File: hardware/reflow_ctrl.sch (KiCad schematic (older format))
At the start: 36 parts, among them IC1 MAX6675, IC2 ATXMEGA128A4U-A, P1 CONN_01X06, P2 CONN_01X02, U1 LT1129CST-3.3, U2 MOC3063, U3 BTA41/600B, X1 USB-Mini-B, X2 Mains, X3 Load

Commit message: Add and assign mains terminal footprint
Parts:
- X2, X3: footprint (none) -> uMIDI:Mains_Solder
- X4: renamed from P2; value CONN_01X02 -> Thermocouple; footprint (none) -> uMIDI:Pinhead1-2
- gave numbers to parts that had none: 1
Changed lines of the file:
@@
 	6300 2450 6500 2450
 $Comp
-L GND #PWR01
+L GND #PWR20
 U 1 1 56A9FAD0
 P 6450 2700
-F 0 "#PWR01" H 6450 2450 50  0001 C CNN
+F 0 "#PWR20" H 6450 2450 50  0001 C CNN
 F 1 "GND" H 6450 2550 50  0000 C CNN
 F 2 "" H 6450 2700 60  0000 C CNN
@@
 $EndComp
 $Comp
-L GND #PWR02
+L GND #PWR22
 U 1 1 56AA0C93
 P 8200 5000
-F 0 "#PWR02" H 8200 4750 50  0001 C CNN
+F 0 "#PWR22" H 8200 4750 50  0001 C CNN
 F 1 "GND" H 8200 4850 50  0000 C CNN
 F 2 "" H 8200 5000 60  0000 C CNN
@@
 	8100 4950 8350 4950
 $Comp
-L +5V #PWR03
+L +5V #PWR21
 U 1 1 56AA1098
 P 8200 4600
-F 0 "#PWR03" H 8200 4450 50  0001 C CNN
+F 0 "#PWR21" H 8200 4450 50  0001 C CNN
 F 1 "+5V" H 8200 4740 50  0000 C CNN
 F 2 "" H 8200 4600 60  0000 C CNN
@@
 U 1 1 56AA462E
 P 8350 4800
-F 0 "C11" H 8250 4700 50  0000 L CNN
-F 1 "100n" H 8100 4900 50  0000 L CNN
+F 0 "C11" H 8350 4900 50  0000 L CNN
+F 1 "100n" H 8350 4700 50  0000 L CNN
 F 2 "Capacitors_SMD:C_0603" H 8388 4650 30  0001 C CNN
 F 3 "" H 8350 4800 60  0001 C CNN
@@
 	2550 2550 2000 2550
 $Comp
-L GND #PWR04
+L GND #PWR5
 U 1 1 56AE5967
 P 2050 3100
-F 0 "#PWR04" H 2050 2850 50  0001 C CNN
+F 0 "#PWR5" H 2050 2850 50  0001 C CNN
 F 1 "GND" H 2050 2950 50  0001 C CNN
 F 2 "" H 2050 3100 60  0000 C CNN
@@
 NoConn ~ 2000 2850
 $Comp
-L GND #PWR05
+L GND #PWR17
 U 1 1 56AE5F8B
 P 3500 5200
-F 0 "#PWR05" H 3500 4950 50  0001 C CNN
+F 0 "#PWR17" H 3500 4950 50  0001 C CNN
 F 1 "GND" H 3500 5050 50  0001 C CNN
 F 2 "" H 3500 5200 60  0000 C CNN
@@
 $EndComp
 $Comp
-L GND #PWR06
+L GND #PWR11
 U 1 1 56AEA13C
 P 2450 2400
-F 0 "#PWR06" H 2450 2150 50  0001 C CNN
+F 0 "#PWR11" H 2450 2150 50  0001 C CNN
 F 1 "GND" H 2450 2250 50  0001 C CNN
 F 2 "" H 2450 2400 60  0000 C CNN
@@
 $EndComp
 $Comp
-L GND #PWR07
+L GND #PWR13
 U 1 1 56AEAD9B
 P 2800 2400
-F 0 "#PWR07" H 2800 2150 50  0001 C CNN
+F 0 "#PWR13" H 2800 2150 50  0001 C CNN
 F 1 "GND" H 2800 2250 50  0001 C CNN
 F 2 "" H 2800 2400 60  0000 C CNN
@@
 $EndComp
 $Comp
-L GND #PWR08
+L GND #PWR15
 U 1 1 56AEADF6
 P 3050 2400
-F 0 "#PWR08" H 3050 2150 50  0001 C CNN
+F 0 "#PWR15" H 3050 2150 50  0001 C CNN
 F 1 "GND" H 3050 2250 50  0001 C CNN
 F 2 "" H 3050 2400 60  0000 C CNN
@@
 $EndComp
 $Comp
-L GND #PWR09
+L GND #PWR16
 U 1 1 56AEAE51
 P 3300 2400
-F 0 "#PWR09" H 3300 2150 50  0001 C CNN
+F 0 "#PWR16" H 3300 2150 50  0001 C CNN
 F 1 "GND" H 3300 2250 50  0001 C CNN
 F 2 "" H 3300 2400 60  0000 C CNN
@@
 	3700 1950 3800 1950
 $Comp
-L GND #PWR010
+L GND #PWR18
 U 1 1 56AEE788
 P 3950 2400
-F 0 "#PWR010" H 3950 2150 50  0001 C CNN
+F 0 "#PWR18" H 3950 2150 50  0001 C CNN
 F 1 "GND" H 3950 2250 50  0001 C CNN
 F 2 "" H 3950 2400 60  0000 C CNN
@@
 $EndComp
 $Comp
-L GND #PWR011
+L GND #PWR19
 U 1 1 56AEE817
 P 4200 2400
-F 0 "#PWR011" H 4200 2150 50  0001 C CNN
+F 0 "#PWR19" H 4200 2150 50  0001 C CNN
 F 1 "GND" H 4200 2250 50  0001 C CNN
 F 2 "" H 4200 2400 60  0000 C CNN
@@
 $EndComp
 $Comp
-L +3.3V #PWR012
+L +3.3V #PWR7
 U 1 1 56AEE96E
 P 2150 1250
-F 0 "#PWR012" H 2150 1100 50  0001 C CNN
+F 0 "#PWR7" H 2150 1100 50  0001 C CNN
 F 1 "+3.3V" H 2150 1390 50  0000 C CNN
 F 2 "" H 2150 1250 60  0000 C CNN
@@
 $EndComp
 $Comp
-L GND #PWR013
+L GND #PWR4
 U 1 1 56AF308D
 P 1800 5700
-F 0 "#PWR013" H 1800 5450 50  0001 C CNN
+F 0 "#PWR4" H 1800 5450 50  0001 C CNN
 F 1 "GND" H 1800 5550 50  0001 C CNN
 F 2 "" H 1800 5700 60  0000 C CNN
@@
 $EndComp
 $Comp
-L GND #PWR014
+L GND #PWR6
 U 1 1 56AF30DC
 P 2100 5700
-F 0 "#PWR014" H 2100 5450 50  0001 C CNN
+F 0 "#PWR6" H 2100 5450 50  0001 C CNN
 F 1 "GND" H 2100 5550 50  0001 C CNN
 F 2 "" H 2100 5700 60  0000 C CNN
@@
 $EndComp
 $Comp
-L GND #PWR015
+L GND #PWR10
 U 1 1 56AF3117
 P 2400 5700
-F 0 "#PWR015" H 2400 5450 50  0001 C CNN
+F 0 "#PWR10" H 2400 5450 50  0001 C CNN
 F 1 "GND" H 2400 5550 50  0001 C CNN
 F 2 "" H 2400 5700 60  0000 C CNN
@@
 	1750 4600 1750 4550
 $Comp
-L GND #PWR016
+L GND #PWR2
 U 1 1 56AF578E
 P 1700 5000
-F 0 "#PWR016" H 1700 4750 50  0001 C CNN
+F 0 "#PWR2" H 1700 4750 50  0001 C CNN
 F 1 "GND" H 1700 4850 50  0001 C CNN
 F 2 "" H 1700 5000 60  0000 C CNN
@@
 	1200 5650 1200 5600
 $Comp
-L GND #PWR017
+L GND #PWR1
 U 1 1 56AF75D9
 P 1300 5700
-F 0 "#PWR017" H 1300 5450 50  0001 C CNN
+F 0 "#PWR1" H 1300 5450 50  0001 C CNN
 F 1 "GND" H 1300 5550 50  0001 C CNN
 F 2 "" H 1300 5700 60  0000 C CNN
@@
 Connection ~ 1800 4600
 $Comp
-L GND #PWR018
+L GND #PWR9
 U 1 1 56AF8D20
 P 2250 4600
-F 0 "#PWR018" H 2250 4350 50  0001 C CNN
+F 0 "#PWR9" H 2250 4350 50  0001 C CNN
 F 1 "GND" H 2250 4450 50  0001 C CNN
 F 2 "" H 2250 4600 60  0000 C CNN
@@
 $EndComp
 $Comp
-L GND #PWR019
+L GND #PWR8
 U 1 1 56AFB955
 P 2200 7500
-F 0 "#PWR019" H 2200 7250 50  0001 C CNN
+F 0 "#PWR8" H 2200 7250 50  0001 C CNN
 F 1 "GND" H 2200 7350 50  0001 C CNN
 F 2 "" H 2200 7500 60  0000 C CNN
@@
 	2200 7500 2200 7450
 $Comp
-L GND #PWR020
+L GND #PWR3
 U 1 1 56AFBD16
 P 1700 7500
-F 0 "#PWR020" H 1700 7250 50  0001 C CNN
+F 0 "#PWR3" H 1700 7250 50  0001 C CNN
 F 1 "GND" H 1700 7350 50  0001 C CNN
 F 2 "" H 1700 7500 60  0000 C CNN
@@
 $EndComp
 $Comp
-L GND #PWR021
+L GND #PWR12
 U 1 1 56AFBD84
 P 2700 7500
-F 0 "#PWR021" H 2700 7250 50  0001 C CNN
+F 0 "#PWR12" H 2700 7250 50  0001 C CNN
 F 1 "GND" H 2700 7350 50  0001 C CNN
 F 2 "" H 2700 7500 60  0000 C CNN
@@
 Connection ~ 2700 7100
 $Comp
-L +3.3V #PWR022
+L +3.3V #PWR14
 U 1 1 56AFC77E
 P 2850 7100
-F 0 "#PWR022" H 2850 6950 50  0001 C CNN
+F 0 "#PWR14" H 2850 6950 50  0001 C CNN
 F 1 "+3.3V" H 2850 7240 50  0000 C CNN
 F 2 "" H 2850 7100 60  0000 C CNN
@@
 $EndComp
 $Comp
-L PWR_FLAG #FLG023
+L PWR_FLAG #FLG1
 U 1 1 56AFC903
 P 1600 7050
-F 0 "#FLG023" H 1600 7145 50  0001 C CNN
+F 0 "#FLG1" H 1600 7145 50  0001 C CNN
 F 1 "PWR_FLAG" H 1600 7230 50  0000 C CNN
 F 2 "" H 1600 7050 60  0000 C CNN
@@
 $EndComp
 $Comp
-L PWR_FLAG #FLG024
+L PWR_FLAG #FLG2
 U 1 1 56AFCDDC
 P 2800 7050
-F 0 "#FLG024" H 2800 7145 50  0001 C CNN
+F 0 "#FLG2" H 2800 7145 50  0001 C CNN
 F 1 "PWR_FLAG" H 2800 7230 50  0000 C CNN
 F 2 "" H 2800 7050 60  0000 C CNN
@@
 F 0 "X2" H 10200 2200 50  0000 C CNN
 F 1 "Mains" V 10300 2000 50  0000 C CNN
-F 2 "" H 10200 2000 60  0000 C CNN
+F 2 "uMIDI:Mains_Solder" H 10200 2000 60  0001 C CNN
 F 3 "" H 10200 2000 60  0000 C CNN
 	1    10200 2000
@@
 F 0 "X3" H 10200 3500 50  0000 C CNN
 F 1 "Load" V 10300 3300 50  0000 C CNN
-F 2 "" H 10200 3300 60  0000 C CNN
+F 2 "uMIDI:Mains_Solder" H 10200 3300 60  0001 C CNN
 F 3 "" H 10200 3300 60  0000 C CNN
 	1    10200 3300
@@
 	9500 3400 10000 3400
 $Comp
-L CONN_01X02 P2
+L CONN_01X02 X4
 U 1 1 56B0080E
 P 9300 4800
-F 0 "P2" H 9300 4950 50  0000 C CNN
-F 1 "CONN_01X02" V 9400 4800 50  0000 C CNN
-F 2 "" H 9300 4800 60  0000 C CNN
+F 0 "X4" H 9300 4950 50  0000 C CNN
+F 1 "Thermocouple" V 9400 4800 50  0000 C CNN
+F 2 "uMIDI:Pinhead1-2" H 9300 4800 60  0001 C CNN
 F 3 "" H 9300 4800 60  0000 C CNN
 	1    9300 4800
@@
 PWR
 $Comp
-L R R?
+L R R7
 U 1 1 56AE5095
 P 8750 2950
-F 0 "R?" V 8830 2950 50  0000 C CNN
+F 0 "R7" V 8830 2950 50  0000 C CNN
 F 1 "47" V 8750 2950 50  0000 C CNN
 F 2 "Resistors_SMD:R_1206" V 8680 2950 30  0001 C CNN

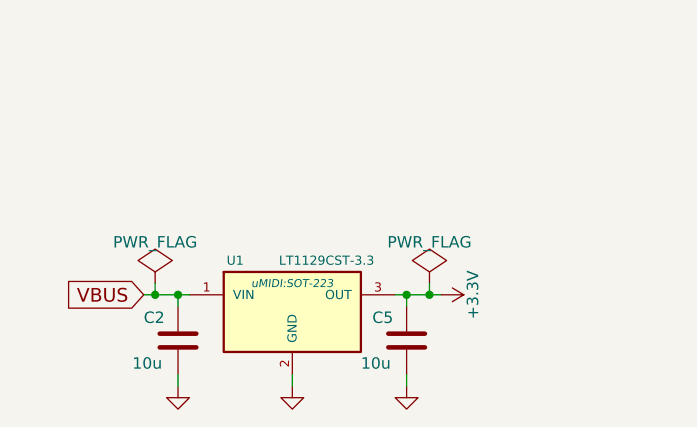
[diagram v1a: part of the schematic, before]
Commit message: Add supplier links and optotriac footprint
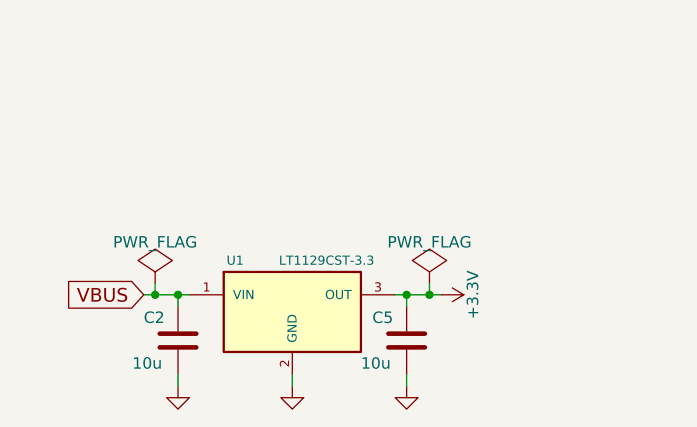
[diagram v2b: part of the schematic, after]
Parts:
- U1: Manufacturer (none) -> Linear Technology; Manufacturer Part Number (none) -> LT1129CST-3.3#PBF; Supplier (none) -> Digikey; Supplier Link (none) -> https://www.digikey.de/product-detail/de/LT1129CST-3.3%23PB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; Supplier Part Number (none) -> LT1129CST-3.3#PBF-ND
- U2: footprint (none) -> uMIDI:MOC3063_SMT; Manufacturer (none) -> Fairchild Semiconductor; Manufacturer Part Number (none) -> MOC3063SR2VM; Supplier (none) -> Digikey; Supplier Link (none) -> http://www.digikey.de/product-detail/de/MOC3063SR2VM/MOC306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; Supplier Part Number (none) -> MOC3063SR2VMCT-ND
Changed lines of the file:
@@
 F 0 "U2" H 6600 2750 50  0000 L CNN
 F 1 "MOC3063" H 6600 2350 50  0000 L CNN
-F 2 "" H 6800 2550 50  0000 L CIN
-F 3 "" H 6775 2550 50  0000 L CNN
+F 2 "uMIDI:MOC3063_SMT" H 6800 2550 50  0001 L CIN
+F 3 "https://www.fairchildsemi.com/datasheets/MO/MOC3061M.pdf" H 6775 2550 50  0001 L CNN
+F 4 "MOC3063SR2VM" H 6600 2750 50  0001 L CNN "Manufacturer Part Number"
+F 5 "MOC3063SR2VMCT-ND" H 6600 2750 50  0001 L CNN "Supplier Part Number"
+F 6 "Fairchild Semiconductor" H 6600 2750 50  0001 L CNN "Manufacturer"
+F 7 "Digikey" H 6600 2750 50  0001 L CNN "Supplier"
+F 8 "http://www.digikey.de/product-detail/de/MOC3063SR2VM/MOC3063SR2VMCT-ND/2094175" H 6600 2750 50  0001 L CNN "Supplier Link"
 	1    6800 2550
 	1    0    0    -1
@@
 F 0 "U1" H 1950 7350 40  0000 C CNN
 F 1 "LT1129CST-3.3" H 2350 7350 40  0000 C CNN
-F 2 "uMIDI:SOT-223" H 2200 7250 35  0000 C CIN
-F 3 "" H 2200 7150 60  0000 C CNN
+F 2 "uMIDI:SOT-223" H 2200 7250 35  0001 C CIN
+F 3 "http://cds.linear.com/docs/en/datasheet/112935ff.pdf" H 2200 7150 60  0001 C CNN
+F 4 "https://www.digikey.de/product-detail/de/LT1129CST-3.3%23PBF/LT1129CST-3.3%23PBF-ND/889181" H 1950 7350 40  0001 C CNN "Supplier Link"
+F 5 "Linear Technology" H 1950 7350 40  0001 C CNN "Manufacturer"
+F 6 "Digikey" H 1950 7350 40  0001 C CNN "Supplier"
+F 7 "LT1129CST-3.3#PBF-ND" H 1950 7350 40  0001 C CNN "Supplier Part Number"
+F 8 "LT1129CST-3.3#PBF" H 1950 7350 40  0001 C CNN "Manufacturer Part Number"
 	1    2200 7150
 	1    0    0    -1

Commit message: Sanetize output circuit; Add varistor
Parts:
- removed L3: 1.5m, symbol INDUCTOR_SMALL
- removed R7: 47, Resistors_SMD:R_1206, symbol R
- added VR1: 430V, Varistors:RV_Disc_D21.5_W5.1_P10, symbol VR
- F1: value F_Small -> Insert 12A slow; footprint (none) -> Fuse_Holders_and_Fuses:Fuseholder5x20_horiz_open_universal_Type-III; Manufacturer (none) -> Schurter Inc.; Manufacturer Part Number (none) -> 0031.8231; Rated Current (none) -> 10A; Supplier (none) -> Digikey; Supplier Link (none) -> http://www.digikey.de/product-detail/de/0031.8231/486-1261-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; Supplier Part Number (none) -> 486-1261-ND
- R4, R5: footprint (none) -> Resistors_SMD:R_1206
- R6: value 47 -> 39
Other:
- moved on the sheet: C12, F1, R6, X2, X3

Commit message: Add fuse holder footprint
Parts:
- F1: footprint Fuse_Holders_and_Fuses:Fuseholder5x20_horiz_open_universal_Type-III -> uMIDI:Fuseholder_Schurter_20x5
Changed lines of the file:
@@
 F 0 "F1" H 9610 1960 50  0000 L CNN
 F 1 "Insert 12A slow" H 9350 1800 50  0000 L CNN
-F 2 "Fuse_Holders_and_Fuses:Fuseholder5x20_horiz_open_universal_Type-III" H 9650 1900 60  0001 C CNN
+F 2 "uMIDI:Fuseholder_Schurter_20x5" H 9650 1900 60  0001 C CNN
 F 3 "http://www.schurterinc.com/var/schurter/storage/ilcatalogue/files/document/datasheet/en/pdf/typ_OGD.pdf" H 9650 1900 60  0001 C CNN
 F 4 "Schurter Inc." H 9610 1960 50  0001 L CNN "Manufacturer"

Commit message: Assign all footprints
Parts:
- C1, L1, L2: footprint (none) -> Capacitors_SMD:C_0603
- IC1: footprint (none) -> Housings_SOIC:SOIC-8_3.9x4.9mm_Pitch1.27mm
- P1: value CONN_01X06 -> PDI; footprint (none) -> Pin_Headers:Pin_Header_Straight_2x03
- R1, R2: footprint (none) -> Resistors_SMD:R_0603
- R3: value TBD -> 390; footprint (none) -> Resistors_SMD:R_0603
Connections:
- wire segments 89 -> 90
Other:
- note added: "Nominal trigger current: 5mA (60mA max)"
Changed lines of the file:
@@
 P 6150 2450
 F 0 "R3" V 6230 2450 50  0000 C CNN
-F 1 "TBD" V 6150 2450 50  0000 C CNN
-F 2 "" V 6080 2450 30  0000 C CNN
+F 1 "390" V 6150 2450 50  0000 C CNN
+F 2 "Resistors_SMD:R_0603" V 6080 2450 30  0001 C CNN
 F 3 "" H 6150 2450 30  0000 C CNN
 	1    6150 2450
@@
 F 0 "IC1" H 7750 5050 60  0000 C CNN
 F 1 "MAX6675" V 7750 4800 50  0000 C CNN
-F 2 "" H 7750 4800 60  0000 C CNN
-F 3 "" H 7750 4800 60  0000 C CNN
+F 2 "Housings_SOIC:SOIC-8_3.9x4.9mm_Pitch1.27mm" H 7750 4800 60  0001 C CNN
+F 3 "http://datasheets.maximintegrated.com/en/ds/MAX6675.pdf" H 7750 4800 60  0001 C CNN
 	1    7750 4800
 	-1   0    0    1
@@
 P 1800 2800
 F 0 "P1" H 1800 3150 50  0000 C CNN
-F 1 "CONN_01X06" V 1900 2800 50  0000 C CNN
-F 2 "" H 1800 2800 60  0000 C CNN
+F 1 "PDI" V 1900 2800 50  0000 C CNN
+F 2 "Pin_Headers:Pin_Header_Straight_2x03" H 1800 2800 60  0001 C CNN
 F 3 "" H 1800 2800 60  0000 C CNN
 	1    1800 2800
@@
 F 0 "L2" V 3500 1950 50  0000 C CNN
 F 1 "Bead 1k@100MHz" V 3350 1950 50  0000 C CNN
-F 2 "" H 3400 1950 60  0000 C CNN
+F 2 "Capacitors_SMD:C_0603" H 3400 1950 60  0001 C CNN
 F 3 "" H 3400 1950 60  0000 C CNN
 	1    3400 1950
@@
 F 0 "L1" H 2250 1650 50  0000 L CNN
 F 1 "10u" H 2250 1550 50  0000 L CNN
-F 2 "" H 2150 1600 60  0000 C CNN
+F 2 "Capacitors_SMD:C_0603" H 2150 1600 60  0001 C CNN
 F 3 "" H 2150 1600 60  0000 C CNN
 	1    2150 1600
@@
 F 0 "R2" V 2380 2800 50  0000 C CNN
 F 1 "10k" V 2300 2800 50  0000 C CNN
-F 2 "" V 2230 2800 30  0000 C CNN
+F 2 "Resistors_SMD:R_0603" V 2230 2800 30  0001 C CNN
 F 3 "" H 2300 2800 30  0000 C CNN
 	1    2300 2800
@@
 F 0 "C1" H 1050 5550 50  0000 L CNN
 F 1 "4.7n" H 1000 5350 50  0000 L CNN
-F 2 "" H 1238 5300 30  0000 C CNN
+F 2 "Capacitors_SMD:C_0603" H 1238 5300 30  0001 C CNN
 F 3 "" H 1200 5450 60  0000 C CNN
 	1    1200 5450
@@
 F 0 "R1" V 1500 5450 50  0000 C CNN
 F 1 "1M" V 1400 5450 50  0000 C CNN
-F 2 "" V 1330 5450 30  0000 C CNN
+F 2 "Resistors_SMD:R_0603" V 1330 5450 30  0001 C CNN
 F 3 "" H 1400 5450 30  0000 C CNN
 	1    1400 5450
@@
 Text Label 4500 4700 0    60   ~ 0
 TC_SO
-Text Label 4650 3450 0    60   ~ 0
+Text Label 4450 2800 0    60   ~ 0
 PWR
 $Comp
@@
 	9250 1900 9250 2300
 Connection ~ 9250 1900
+Wire Wire Line
+	4400 2800 4650 2800
+Text Notes 5050 2300 0    60   ~ 0
+Nominal trigger current: 5mA (60mA max)
 $EndSCHEMATC

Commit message: Initial placement; Select pcb outline; Add TODO
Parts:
- added HS1: HEATSINK, symbol HEATSINK
- U3: Manufacturer (none) -> STMicroelectronics; Manufacturer Part Number (none) -> BTA41-600BRG; Supplier (none) -> Digikey; Supplier Link (none) -> http://www.digikey.de/product-detail/de/BTA41-600BRG/497-24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; Supplier Part Number (none) -> 497-2431-5-ND
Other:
- note added: "TODO\n* Complete supplier links\n* Add 3 Switches and approx. 3 LEDs\n* Replace USB connector by large type B (THT style)\n* Select Heatsink\n* Add netclasses"
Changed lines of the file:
@@
 F 1 "BTA41/600B" H 7750 2200 50  0000 C CNN
 F 2 "TO_SOT_Packages_THT:TO-247_Vertical_Neutral123_largePads" H 8050 2450 60  0001 C CNN
-F 3 "" H 8050 2450 60  0000 C CNN
+F 3 "http://www.st.com/web/en/resource/technical/document/datasheet/CD00002263.pdf" H 8050 2450 60  0001 C CNN
+F 4 "http://www.digikey.de/product-detail/de/BTA41-600BRG/497-2431-5-ND/603456" H 7800 2800 50  0001 C CNN "Supplier Link"
+F 5 "STMicroelectronics" H 7800 2800 50  0001 C CNN "Manufacturer"
+F 6 "Digikey" H 7800 2800 50  0001 C CNN "Supplier"
+F 7 "BTA41-600BRG" H 7800 2800 50  0001 C CNN "Manufacturer Part Number"
+F 8 "497-2431-5-ND" H 7800 2800 50  0001 C CNN "Supplier Part Number"
 	1    8050 2450
 	1    0    0    -1
@@
 Text Notes 5050 2300 0    60   ~ 0
 Nominal trigger current: 5mA (60mA max)
+$Comp
+L HEATSINK HS1
+U 1 1 56B07BF1
+P 8050 1750
+F 0 "HS1" H 8050 1950 50  0000 C CNN
+F 1 "HEATSINK" H 8050 1700 50  0000 C CNN
+F 2 "" H 8050 1750 60  0000 C CNN
+F 3 "" H 8050 1750 60  0000 C CNN
+	1    8050 1750
+	1    0    0    -1
+$EndComp
+Text Notes 4000 6750 0    60   ~ 0
+TODO\n* Complete supplier links\n* Add 3 Switches and approx. 3 LEDs\n* Replace USB connector by large type B (THT style)\n* Select Heatsink\n* Add netclasses
 $EndSCHEMATC
